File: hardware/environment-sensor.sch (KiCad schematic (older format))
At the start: 0 parts

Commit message: Almost finished layout
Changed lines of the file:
@@
 LIBS:valves
 LIBS:wiznet
-LIBS:Sensors_STMicroelectronics
 LIBS:Sensors_Bosch
 LIBS:environment-sensor-cache
@@
 F2 "SS_PHY" O R 6050 5150 60
 F3 "SCLK" O R 6050 5350 60
-F4 "RESET" O R 6050 5250 60
+F4 "~RESET" O R 6050 5250 60
 F5 "MISO" O R 6050 5450 60
 F6 "MOSI" O R 6050 5550 60
@@
 F0 "Network I/O" 60
 F1 "network.sch" 60
-F2 "RESET" I L 7300 3300 60
+F2 "~RESET" I L 7300 3300 60
 F3 "SS_PHY" I L 7300 3200 60
 F4 "MOSI" I L 7300 3600 60
@@
 Wire Wire Line
 	7300 5725 6050 5725
+Wire Wire Line
+	6050 5150 6450 5150
+Wire Wire Line
+	6450 5150 6450 3200
+Wire Wire Line
+	6450 3200 7300 3200
+Wire Wire Line
+	6050 5250 6550 5250
+Wire Wire Line
+	6550 5250 6550 3300
+Wire Wire Line
+	6550 3300 7300 3300
+Wire Wire Line
+	7300 3400 6650 3400
+Wire Wire Line
+	6650 3400 6650 5350
+Connection ~ 6650 5350
+Wire Wire Line
+	7300 3500 6750 3500
+Wire Wire Line
+	6750 3500 6750 5450
+Wire Wire Line
+	6750 5450 6050 5450
+Wire Wire Line
+	7300 3600 6850 3600
+Wire Wire Line
+	6850 3600 6850 5550
+Wire Wire Line
+	6850 5550 6050 5550
 $EndSCHEMATC

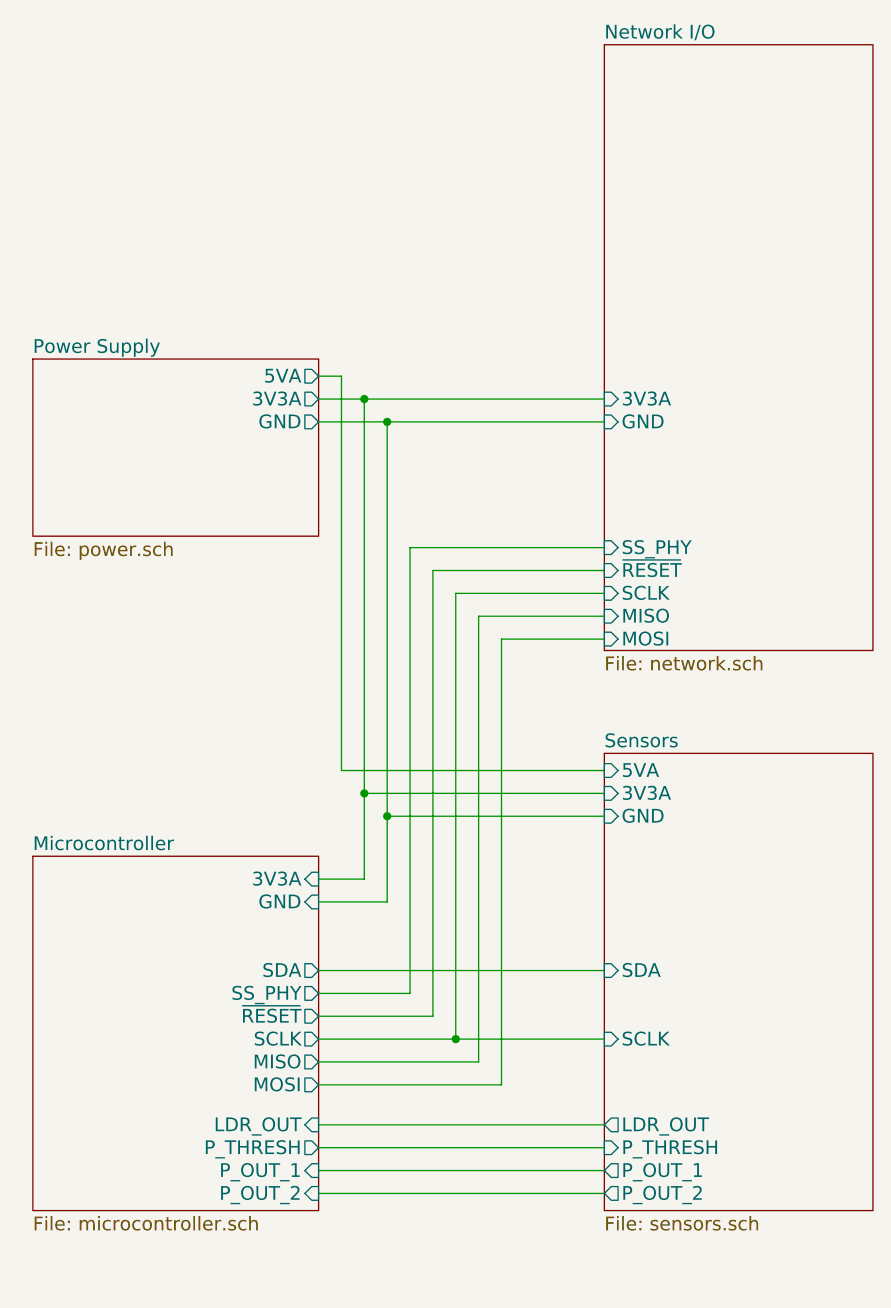
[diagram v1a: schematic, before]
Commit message: Revision of board to address issues
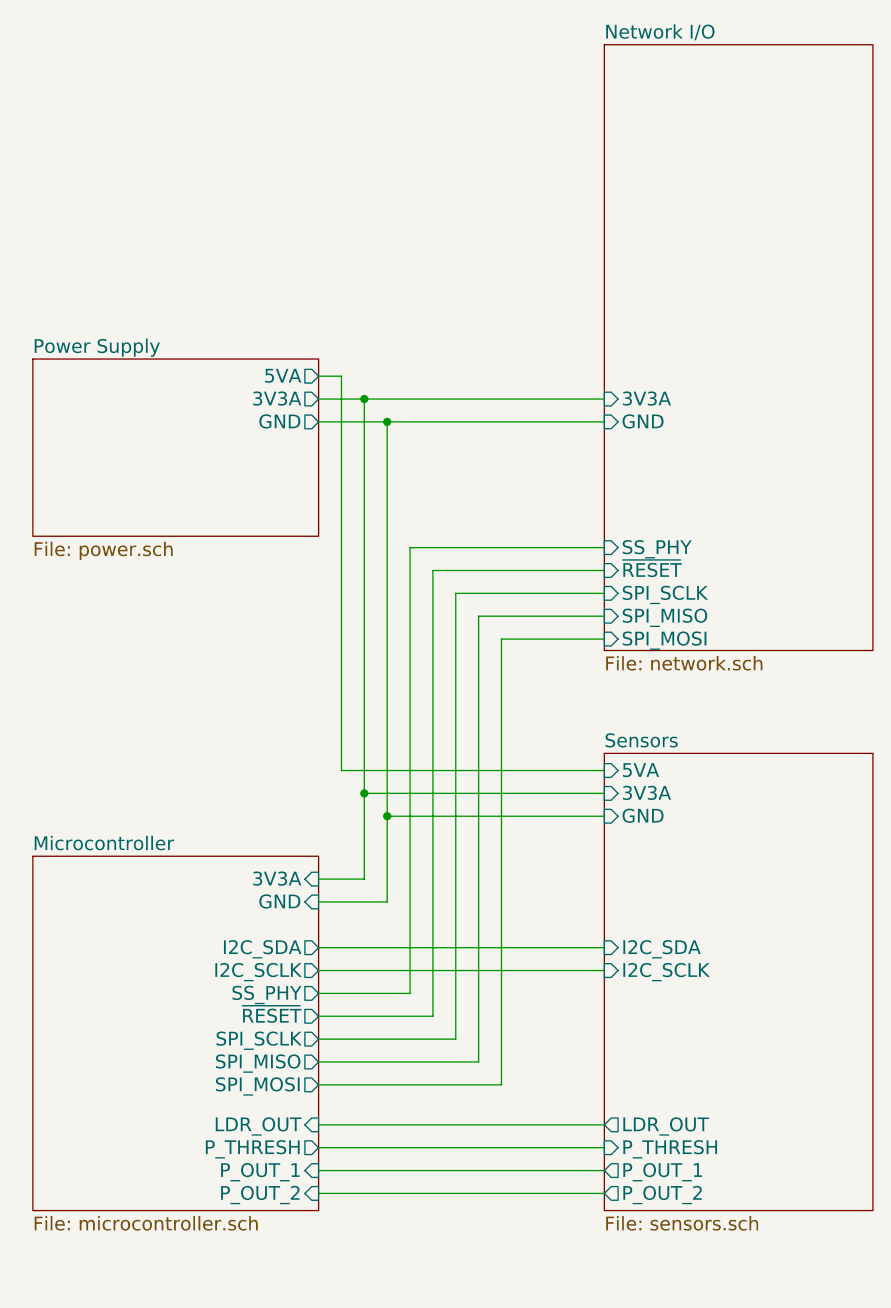
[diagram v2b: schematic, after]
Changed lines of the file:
@@
 LIBS:wiznet
 LIBS:Sensors_Bosch
+LIBS:cetus
 LIBS:environment-sensor-cache
 EELAYER 25 0
@@
 F1 "microcontroller.sch" 60
 F2 "SS_PHY" O R 6050 5150 60
-F3 "SCLK" O R 6050 5350 60
+F3 "SPI_SCLK" O R 6050 5350 60
 F4 "~RESET" O R 6050 5250 60
-F5 "MISO" O R 6050 5450 60
-F6 "MOSI" O R 6050 5550 60
-F7 "SDA" O R 6050 5050 60
+F5 "SPI_MISO" O R 6050 5450 60
+F6 "SPI_MOSI" O R 6050 5550 60
+F7 "I2C_SDA" O R 6050 4950 60
 F8 "3V3A" I R 6050 4650 60
 F9 "GND" I R 6050 4750 60
@@
 F12 "P_OUT_2" I R 6050 6025 60
 F13 "LDR_OUT" I R 6050 5725 60
+F14 "I2C_SCLK" O R 6050 5050 60
 $EndSheet
 $Sheet
@@
 F2 "~RESET" I L 7300 3300 60
 F3 "SS_PHY" I L 7300 3200 60
-F4 "MOSI" I L 7300 3600 60
-F5 "MISO" I L 7300 3500 60
-F6 "SCLK" I L 7300 3400 60
+F4 "SPI_MOSI" I L 7300 3600 60
+F5 "SPI_MISO" I L 7300 3500 60
+F6 "SPI_SCLK" I L 7300 3400 60
 F7 "GND" I L 7300 2650 60
 F8 "3V3A" I L 7300 2550 60
@@
 F1 "sensors.sch" 60
 F2 "GND" I L 7300 4375 60
-F3 "SCLK" I L 7300 5350 60
-F4 "SDA" I L 7300 5050 60
+F3 "I2C_SCLK" I L 7300 5050 60
+F4 "I2C_SDA" I L 7300 4950 60
 F5 "3V3A" I L 7300 4275 60
 F6 "5VA" I L 7300 4175 60
@@
 $EndSheet
 Wire Wire Line
-	6050 5050 7300 5050
+	6050 4950 7300 4950
 Wire Wire Line
-	6050 5350 7300 5350
+	6050 5350 6650 5350
 Wire Wire Line
 	7300 4275 6250 4275
@@
 Wire Wire Line
 	6650 3400 6650 5350
-Connection ~ 6650 5350
 Wire Wire Line
 	7300 3500 6750 3500
@@
 Wire Wire Line
 	6850 5550 6050 5550
+Wire Wire Line
+	7300 5050 6050 5050
 $EndSCHEMATC

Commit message: New revision to board
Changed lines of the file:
@@
 LIBS:Sensors_Bosch
 LIBS:cetus
+LIBS:LDRs_NSL
 LIBS:environment-sensor-cache
 EELAYER 25 0
@@
 $EndDescr
 $Sheet
-S 4800 4550 1250 1550
+S 5275 2375 525  350
+U 58713E48
+F0 "Power Supply" 60
+F1 "power.sch" 60
+F2 "3V3A" O R 5800 2550 60
+F3 "GND" O R 5800 2650 60
+F4 "5VA" O R 5800 2450 60
+$EndSheet
+Wire Wire Line
+	5800 4950 7300 4950
+Wire Wire Line
+	6250 2550 6250 4650
+Wire Wire Line
+	5800 4650 6250 4650
+Wire Wire Line
+	6250 4650 7300 4650
+Wire Wire Line
+	5800 4750 6350 4750
+Wire Wire Line
+	6350 4750 7300 4750
+Wire Wire Line
+	5800 2550 6250 2550
+Wire Wire Line
+	6250 2550 7300 2550
+Wire Wire Line
+	5800 2650 6350 2650
+Wire Wire Line
+	6350 2650 7300 2650
+Connection ~ 6250 2550
+Connection ~ 6350 2650
+Wire Wire Line
+	5800 2450 6150 2450
+Wire Wire Line
+	6150 2450 6150 4550
+Wire Wire Line
+	6450 5150 5800 5150
+Wire Wire Line
+	6450 2850 6450 5150
+Wire Wire Line
+	6550 5250 5800 5250
+Wire Wire Line
+	6550 2950 6550 5250
+Wire Wire Line
+	6750 3150 6750 5450
+Wire Wire Line
+	6850 3250 6850 5550
+Wire Wire Line
+	6950 3350 6950 5650
+Wire Wire Line
+	7300 5050 5800 5050
+$Sheet
+S 7300 2475 1000 950
+U 5870F6A9
+F0 "Network I/O" 60
+F1 "network.sch" 60
+F2 "~PHY_RESET" I L 7300 2950 60
+F3 "PHY_SS" I L 7300 2850 60
+F4 "SPI_MOSI" I L 7300 3350 60
+F5 "SPI_MISO" I L 7300 3250 60
+F6 "SPI_SCLK" I L 7300 3150 60
+F7 "GND" I L 7300 2650 60
+F8 "3V3A" I L 7300 2550 60
+F9 "~PHY_INTERRUPT" O L 7300 3050 60
+$EndSheet
+Wire Wire Line
+	7300 3350 6950 3350
+Wire Wire Line
+	6850 3250 7300 3250
+Wire Wire Line
+	7300 3150 6750 3150
+Wire Wire Line
+	6550 2950 7300 2950
+Wire Wire Line
+	7300 2850 6450 2850
+Wire Wire Line
+	7300 3050 6650 3050
+Wire Wire Line
+	6650 3050 6650 5350
+Wire Wire Line
+	6650 5350 5800 5350
+Wire Wire Line
+	7300 5850 5800 5850
+Wire Wire Line
+	5800 5950 7300 5950
+Wire Wire Line
+	7300 6050 5800 6050
+Wire Wire Line
+	5800 6150 7300 6150
+Wire Wire Line
+	6750 5450 5800 5450
+Wire Wire Line
+	6850 5550 5800 5550
+Wire Wire Line
+	6950 5650 5800 5650
+$Sheet
+S 4800 4475 1000 1850
 U 5870F3CD
 F0 "Microcontroller" 60
 F1 "microcontroller.sch" 60
-F2 "SS_PHY" O R 6050 5150 60
-F3 "SPI_SCLK" O R 6050 5350 60
-F4 "~RESET" O R 6050 5250 60
-F5 "SPI_MISO" O R 6050 5450 60
-F6 "SPI_MOSI" O R 6050 5550 60
-F7 "I2C_SDA" O R 6050 4950 60
-F8 "3V3A" I R 6050 4650 60
-F9 "GND" I R 6050 4750 60
-F10 "P_THRESH" O R 6050 5825 60
-F11 "P_OUT_1" I R 6050 5925 60
-F12 "P_OUT_2" I R 6050 6025 60
-F13 "LDR_OUT" I R 6050 5725 60
-F14 "I2C_SCLK" O R 6050 5050 60
+F2 "PHY_SS" O R 5800 5150 60
+F3 "SPI_SCLK" O R 5800 5450 60
+F4 "SPI_MISO" O R 5800 5550 60
+F5 "SPI_MOSI" O R 5800 5650 60
+F6 "I2C_SDA" B R 5800 4950 60
+F7 "3V3A" I R 5800 4650 60
+F8 "GND" I R 5800 4750 60
+F9 "DUST_1" I R 5800 5950 60
+F10 "DUST_2" I R 5800 6050 60
+F11 "LDR" I R 5800 5850 60
+F12 "I2C_SCLK" O R 5800 5050 60
+F13 "DUST_2_THRESH" O R 5800 6150 60
+F14 "~PHY_RESET" O R 5800 5250 60
+F15 "~PHY_INTERRUPT" I R 5800 5350 60
+F16 "5VA" I R 5800 4550 60
+F17 "DS18B20" B R 5800 6250 60
 $EndSheet
+Wire Wire Line
+	5800 4550 6150 4550
+Wire Wire Line
+	6150 4550 7300 4550
+Wire Wire Line
+	6350 2650 6350 4750
+Connection ~ 6150 4550
+Connection ~ 6250 4650
+Connection ~ 6350 4750
 $Sheet
-S 7300 1000 1175 2650
-U 5870F6A9
-F0 "Network I/O" 60
-F1 "network.sch" 60
-F2 "~RESET" I L 7300 3300 60
-F3 "SS_PHY" I L 7300 3200 60
-F4 "SPI_MOSI" I L 7300 3600 60
-F5 "SPI_MISO" I L 7300 3500 60
-F6 "SPI_SCLK" I L 7300 3400 60
-F7 "GND" I L 7300 2650 60
-F8 "3V3A" I L 7300 2550 60
-$EndSheet
-$Sheet
-S 7300 4100 1175 2000
+S 7300 4475 1000 1850
 U 58710409
 F0 "Sensors" 60
 F1 "sensors.sch" 60
-F2 "GND" I L 7300 4375 60
+F2 "GND" I L 7300 4750 60
 F3 "I2C_SCLK" I L 7300 5050 60
-F4 "I2C_SDA" I L 7300 4950 60
-F5 "3V3A" I L 7300 4275 60
-F6 "5VA" I L 7300 4175 60
-F7 "P_OUT_2" O L 7300 6025 60
-F8 "P_OUT_1" O L 7300 5925 60
-F9 "P_THRESH" I L 7300 5825 60
-F10 "LDR_OUT" O L 7300 5725 60
-$EndSheet
-$Sheet
-S 4800 2375 1250 775
-U 58713E48
-F0 "Power Supply" 60
-F1 "power.sch" 60
-F2 "3V3A" O R 6050 2550 60
-F3 "GND" O R 6050 2650 60
-F4 "5VA" O R 6050 2450 60
+F4 "I2C_SDA" B L 7300 4950 60
+F5 "3V3A" I L 7300 4650 60
+F6 "5VA" I L 7300 4550 60
+F7 "DUST_2" O L 7300 6050 60
+F8 "DUST_1" O L 7300 5950 60
+F9 "DUST_2_THRESH" I L 7300 6150 60
+F10 "LDR" O L 7300 5850 60
+F11 "DS18B20" B L 7300 6250 60
 $EndSheet
 Wire Wire Line
-	6050 4950 7300 4950
-Wire Wire Line
-	6050 5350 6650 5350
-Wire Wire Line
-	7300 4275 6250 4275
-Wire Wire Line
-	6250 2550 6250 4650
-Wire Wire Line
-	6250 4650 6050 4650
-Wire Wire Line
-	6350 4750 6050 4750
-Wire Wire Line
-	6350 2650 6350 4750
-Wire Wire Line
-	6350 4375 7300 4375
-Wire Wire Line
-	6050 2550 7300 2550
-Connection ~ 6250 4275
-Wire Wire Line
-	6050 2650 7300 2650
-Connection ~ 6350 4375
-Connection ~ 6250 2550
-Connection ~ 6350 2650
-Wire Wire Line
-	6050 2450 6150 2450
-Wire Wire Line
-	6150 2450 6150 4175
-Wire Wire Line
-	6150 4175 7300 4175
-Wire Wire Line
-	7300 5825 6050 5825
-Wire Wire Line
-	6050 5925 7300 5925
-Wire Wire Line
-	7300 6025 6050 6025
-Wire Wire Line
-	7300 5725 6050 5725
-Wire Wire Line
-	6050 5150 6450 5150
-Wire Wire Line
-	6450 5150 6450 3200
-Wire Wire Line
-	6450 3200 7300 3200
-Wire Wire Line
-	6050 5250 6550 5250
-Wire Wire Line
-	6550 5250 6550 3300
-Wire Wire Line
-	6550 3300 7300 3300
-Wire Wire Line
-	7300 3400 6650 3400
-Wire Wire Line
-	6650 3400 6650 5350
-Wire Wire Line
-	7300 3500 6750 3500
-Wire Wire Line
-	6750 3500 6750 5450
-Wire Wire Line
-	6750 5450 6050 5450
-Wire Wire Line
-	7300 3600 6850 3600
-Wire Wire Line
-	6850 3600 6850 5550
-Wire Wire Line
-	6850 5550 6050 5550
-Wire Wire Line
-	7300 5050 6050 5050
+	7300 6250 5800 6250
 $EndSCHEMATC

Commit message: Added some part numbers to the schematic
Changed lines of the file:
@@
 	6250 2550 6250 4650
 Wire Wire Line
-	5800 4650 6250 4650
+	5800 4650 7300 4650
 Wire Wire Line
-	6250 4650 7300 4650
+	5800 4750 7300 4750
 Wire Wire Line
-	5800 4750 6350 4750
+	5800 2550 7300 2550
 Wire Wire Line
-	6350 4750 7300 4750
-Wire Wire Line
-	5800 2550 6250 2550
-Wire Wire Line
-	6250 2550 7300 2550
-Wire Wire Line
-	5800 2650 6350 2650
-Wire Wire Line
-	6350 2650 7300 2650
+	5800 2650 7300 2650
 Connection ~ 6250 2550
 Connection ~ 6350 2650
@@
 $EndSheet
 Wire Wire Line
-	5800 4550 6150 4550
-Wire Wire Line
-	6150 4550 7300 4550
+	5800 4550 7300 4550
 Wire Wire Line
 	6350 2650 6350 4750
